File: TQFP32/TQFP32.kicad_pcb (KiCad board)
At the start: 2 copper layers, 20.1 x 40.6 mm, 8 parts, among them J1 Conn_01x16, J2 Conn_01x16, J3 Conn_02x16_Counter_Clockwise, J4 Conn_02x16_Counter_Clockwise

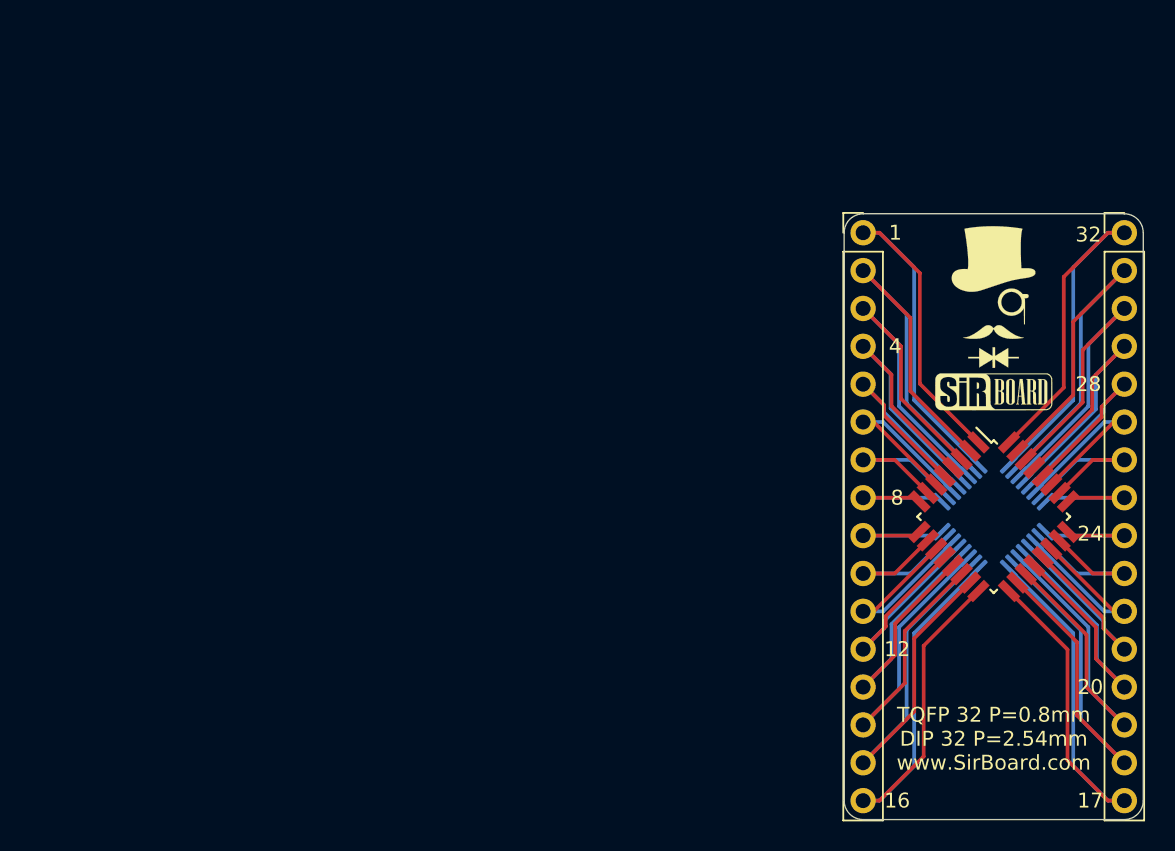
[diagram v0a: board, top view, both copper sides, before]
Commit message: Silkscreens and sizes updated
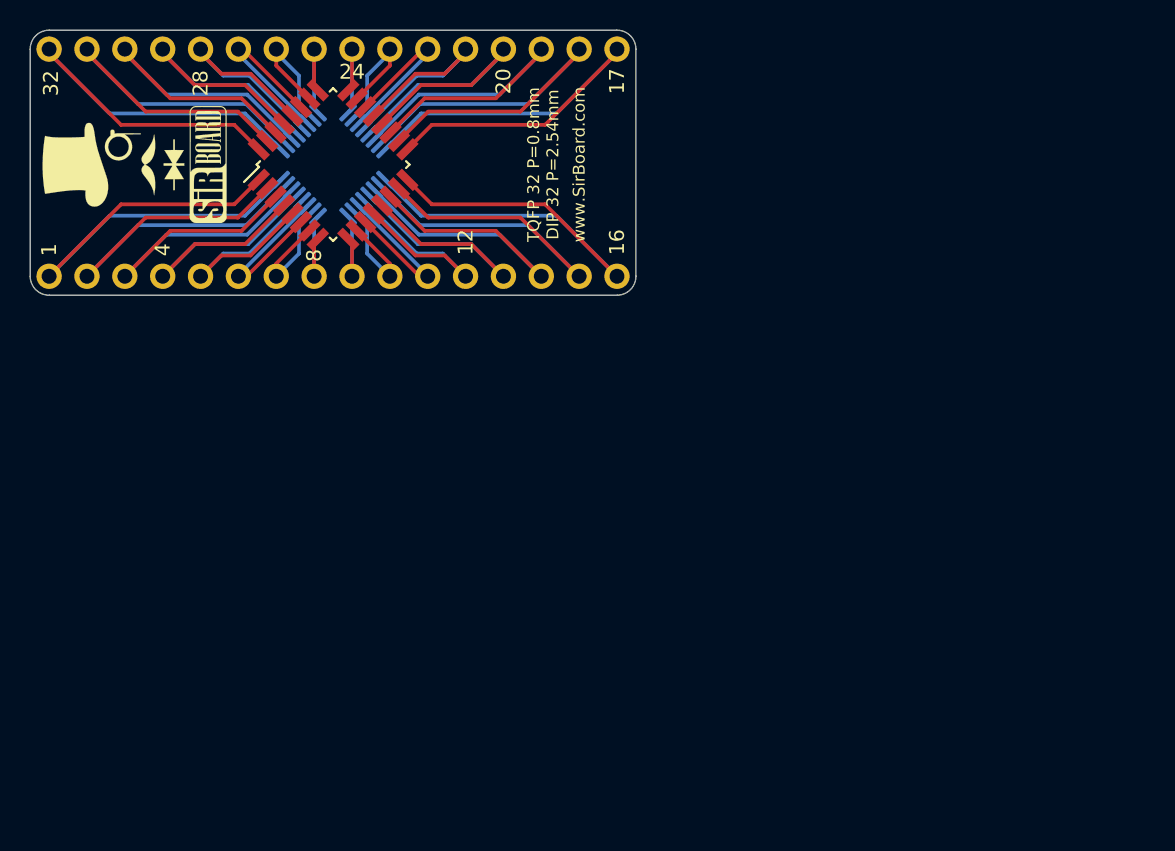
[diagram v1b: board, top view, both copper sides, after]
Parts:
- moved J2 73.2 mm to (136.1, 81.2), turned to 90 degrees
- moved G*** 59.7 mm to (140.5, 88.9), turned to 90 degrees
- moved G*** 54.9 mm to (146.8, 88.9), turned to 90 degrees
- moved J1 54.7 mm to (136.1, 96.4), turned to 90 degrees
- moved J3 50.2 mm to (155.2, 88.9), turned to 45 degrees
- moved J4 50.2 mm to (155.2, 88.9), turned to 135 degrees
- moved G*** 49.2 mm to (161.5, 88.9), turned to 90 degrees
- moved G*** 48.9 mm to (169.3, 88.9), turned to 90 degrees
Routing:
- net Net-(J1-Pad8): track 9.27 -> 6.73 mm
- net Net-(J1-Pad9): track 9.27 -> 6.73 mm
- net Net-(J2-Pad10): track 11.9 -> 9.37 mm
- net Net-(J1-Pad10): track 11.9 -> 9.37 mm
- net Net-(J2-Pad8): track 9.27 -> 6.73 mm
- net Net-(J2-Pad9): track 9.27 -> 6.73 mm
- net Net-(J2-Pad7): track 11.9 -> 9.37 mm
- net Net-(J1-Pad7): track 11.9 -> 9.37 mm
- net Net-(J1-Pad1): track 37.3 -> 35.0 mm
- net Net-(J1-Pad16): track 37.3 -> 35.0 mm
- net Net-(J2-Pad1): track 37.3 -> 35.0 mm
- net Net-(J2-Pad16): track 37.3 -> 35.0 mm
- net Net-(J2-Pad6): track 14.6 -> 12.3 mm
- net Net-(J2-Pad11): track 14.6 -> 12.3 mm
- net Net-(J1-Pad6): track 14.6 -> 12.3 mm
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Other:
- board size 20.1 x 40.6 mm -> 40.6 x 17.8 mm

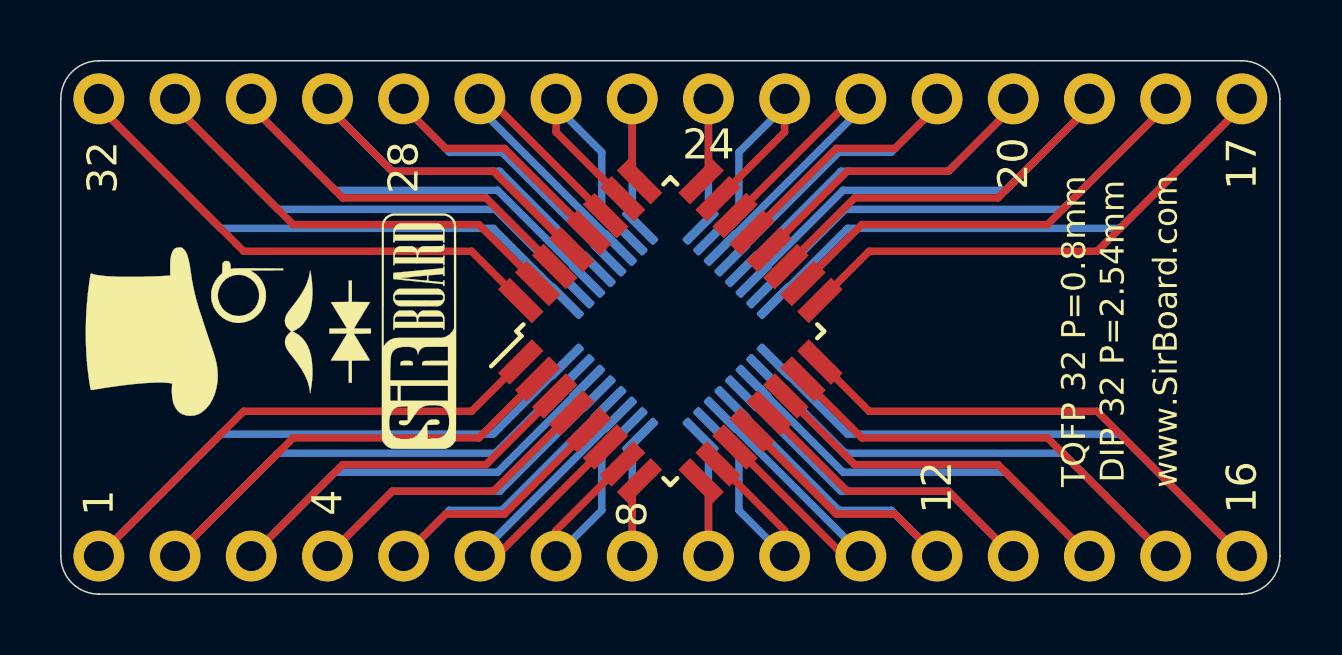
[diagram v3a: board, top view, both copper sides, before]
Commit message: Pin Numbering edited
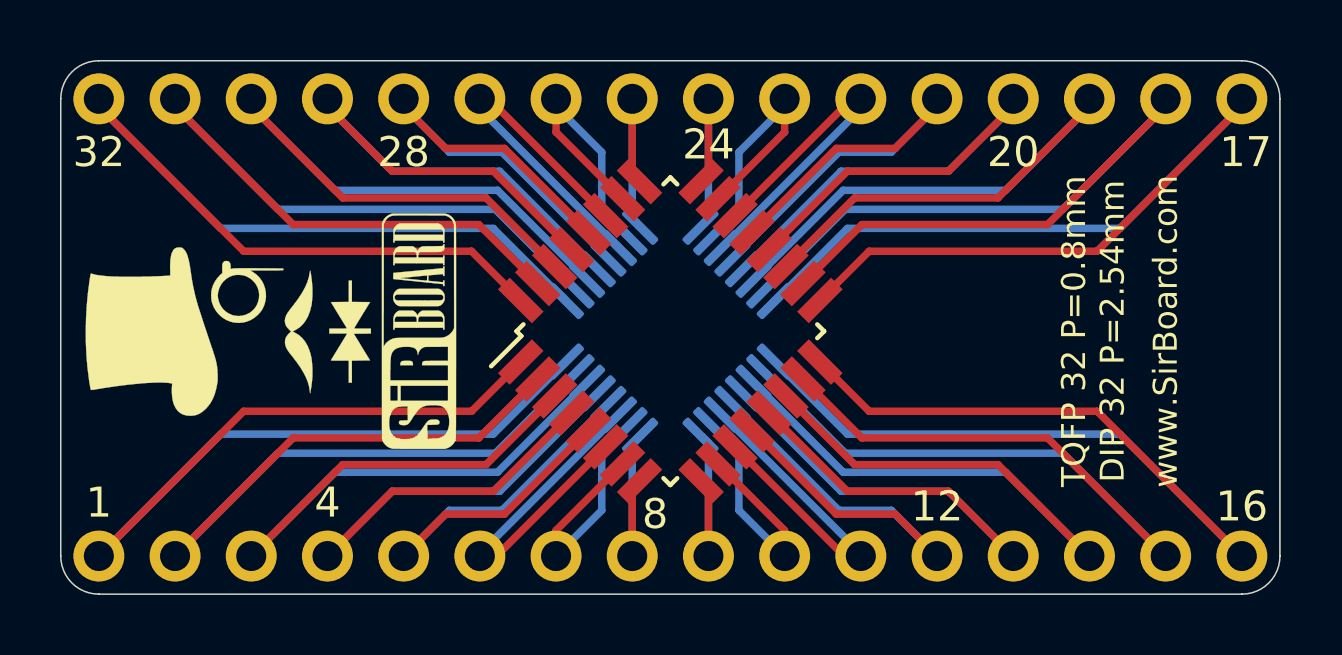
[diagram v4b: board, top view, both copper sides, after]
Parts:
- J1, J2: moved to B.Cu
- turned J1 to 270 degrees
- turned J2 to 270 degrees

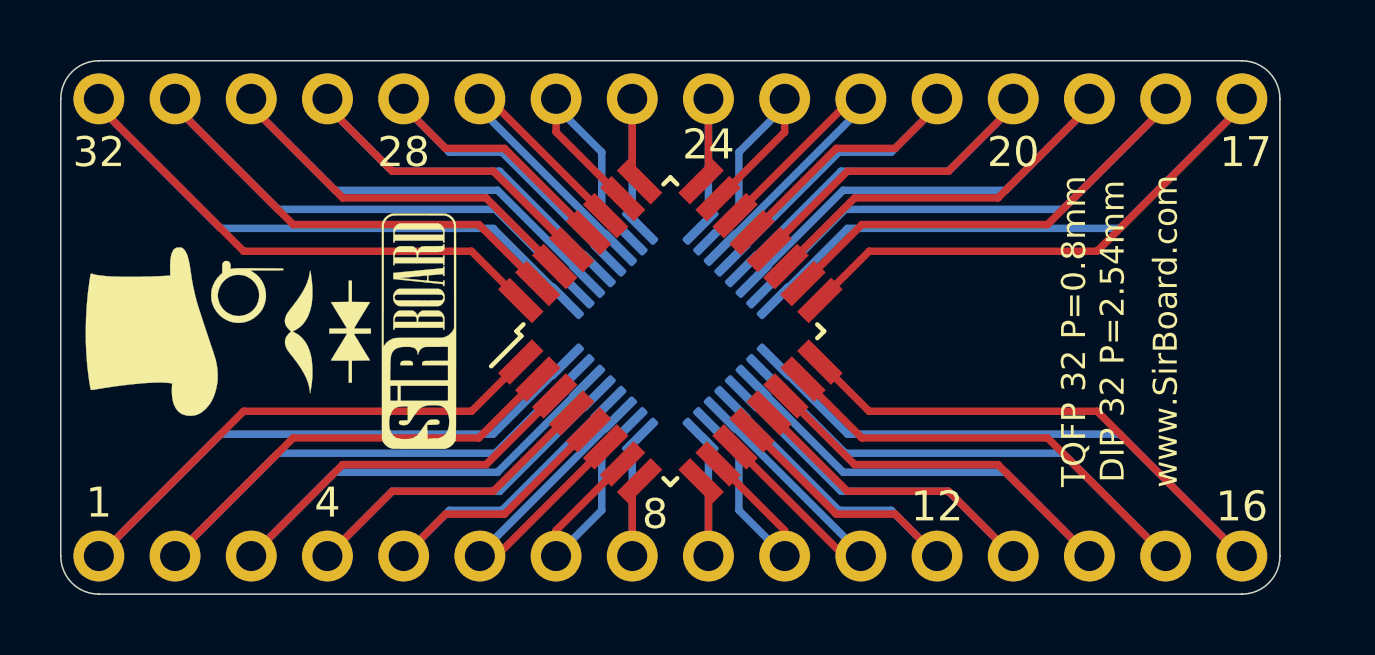
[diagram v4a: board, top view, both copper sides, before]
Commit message: Numbering Orientation Edited
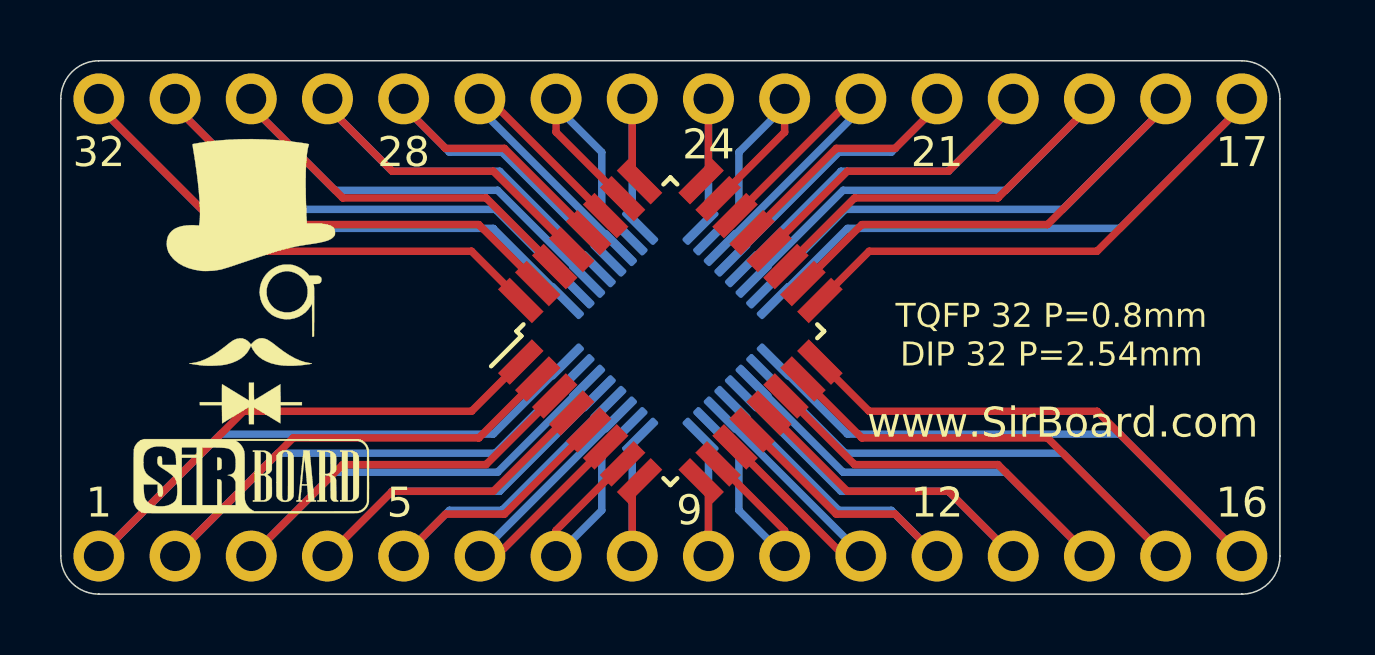
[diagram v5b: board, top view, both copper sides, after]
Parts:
- removed the G*** at (161.5, 88.9)
- added G***: LOGO, logo:SirBoard79x25, B.Cu at (169.2, 93.6)
- moved G*** 7.38 mm to (141.2, 93.7), turned to 0 degrees
- moved G*** 1.82 mm to (141.2, 87.2), turned to 0 degrees
- moved G*** 1.78 mm to (169.2, 87.1), turned to 180 degrees
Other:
- board text added: "21"
- board text added: "5"
- board text added: "9"
- board text removed: "20"
- board text removed: "4"
- board text removed: "8"

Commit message: Silkscreen Edits
Dimensions moved to Drawings Layer
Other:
- rule pad_to_mask_clearance: 0.051 -> 0
- rule solder_mask_min_width: 0.25 -> 0.1
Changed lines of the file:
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@@
     (pad_size 1.7 1.7)
     (pad_drill 1)
-    (pad_to_mask_clearance 0.051)
-    (solder_mask_min_width 0.25)
+    (pad_to_mask_clearance 0)
+    (solder_mask_min_width 0.1)
     (aux_axis_origin 0 0)
     (visible_elements 7FFFFFFF)
@@
       (usegerberadvancedattributes false)
       (creategerberjobfile false)
-      (excludeedgelayer false)
+      (excludeedgelayer true)
       (linewidth 0.100000)
       (plotframeref false)
       (viasonmask false)
       (mode 1)
-      (useauxorigin false)
+      (useauxorigin true)
       (hpglpennumber 1)
       (hpglpenspeed 20)
@@
       (psnegative false)
       (psa4output false)
-      (plotreference false)
-      (plotvalue true)
+      (plotreference true)
+      (plotvalue false)
       (plotinvisibletext false)
       (padsonsilk false)
@@
     )
   )
-  (dimension 38.1 (width 0.15) (layer F.SilkS)
-    (gr_text "38.100 mm" (at 155.194 77.567) (layer F.SilkS)
+  (dimension 38.1 (width 0.15) (layer Dwgs.User)
+    (gr_text "38.100 mm" (at 155.194 77.567) (layer Dwgs.User)
       (effects (font (size 1 1) (thickness 0.15)) hide)
     )
@@
     (arrow2b (pts (xy 136.144 78.867) (xy 137.270504 78.280579)))
   )
-  (dimension 40.64 (width 0.15) (layer F.SilkS)
-    (gr_text "40.640 mm" (at 155.194 74.773) (layer F.SilkS)
+  (dimension 40.64 (width 0.15) (layer Dwgs.User)
+    (gr_text "40.640 mm" (at 155.194 74.773) (layer Dwgs.User)
       (effects (font (size 1 1) (thickness 0.15)) hide)
     )
@@
     (arrow2b (pts (xy 134.874 76.073) (xy 136.000504 75.486579)))
   )
-  (dimension 15.24 (width 0.12) (layer F.SilkS)
-    (gr_text "15.240 mm" (at 131.318 88.773 90) (layer F.SilkS)
+  (dimension 15.24 (width 0.12) (layer Dwgs.User)
+    (gr_text "15.240 mm" (at 131.318 88.773 90) (layer Dwgs.User)
       (effects (font (size 1 1) (thickness 0.15)) hide)
     )
@@
     (arrow2b (pts (xy 132.588 96.393) (xy 132.001579 95.266496)))
   )
-  (dimension 17.78 (width 0.12) (layer F.SilkS)
-    (gr_text "17.780 mm" (at 128.778 88.773 90) (layer F.SilkS)
+  (dimension 17.78 (width 0.12) (layer Dwgs.User)
+    (gr_text "17.780 mm" (at 128.778 88.773 90) (layer Dwgs.User)
       (effects (font (size 1 1) (thickness 0.15)) hide)
     )

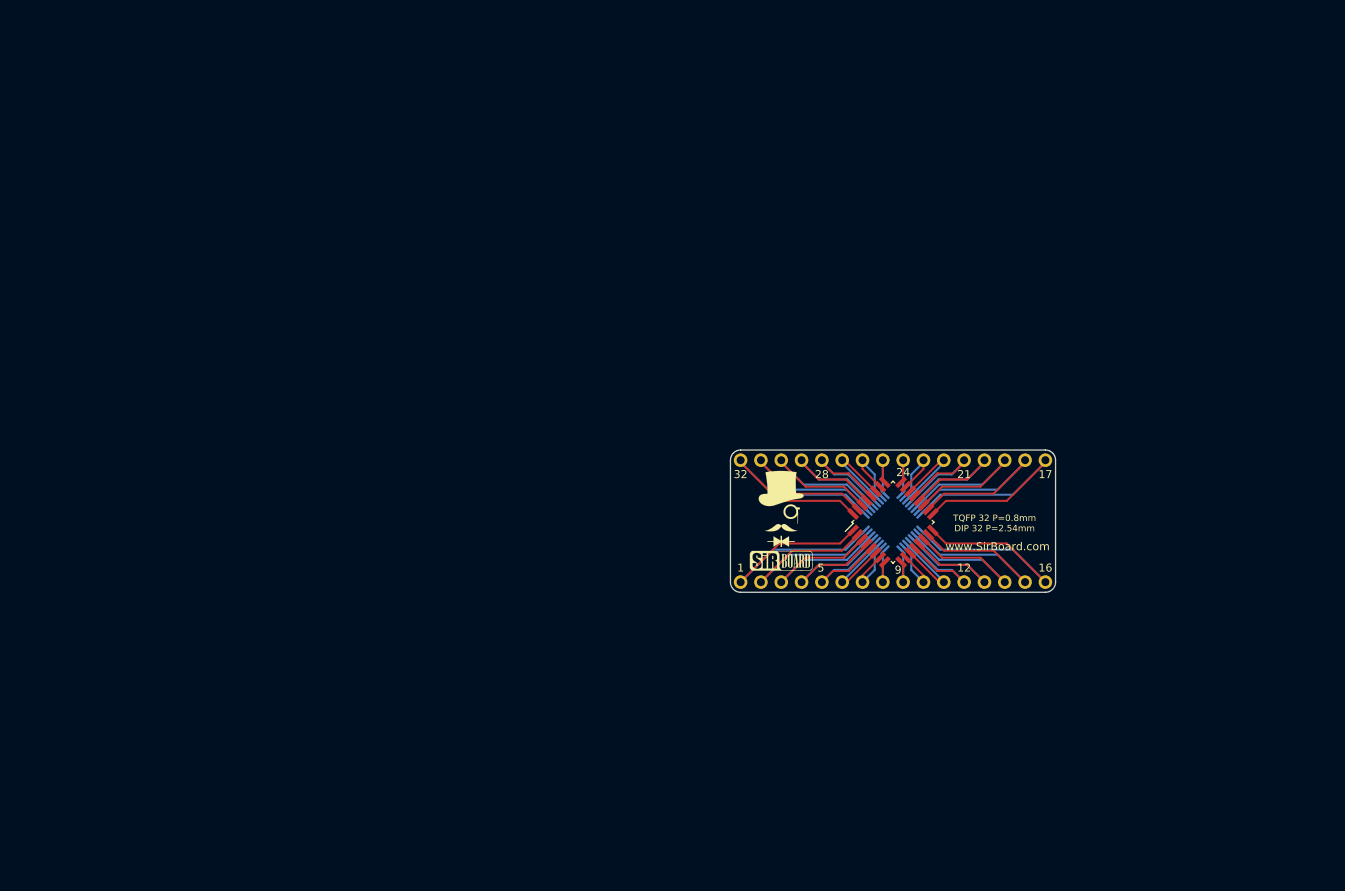
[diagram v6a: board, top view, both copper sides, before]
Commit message: USB, SD and CR Cells Added
MicroSD, MicroUSB, MiniUSB, USB-C, CR1220, CR2032 added as well as all schematics page sizes optimised
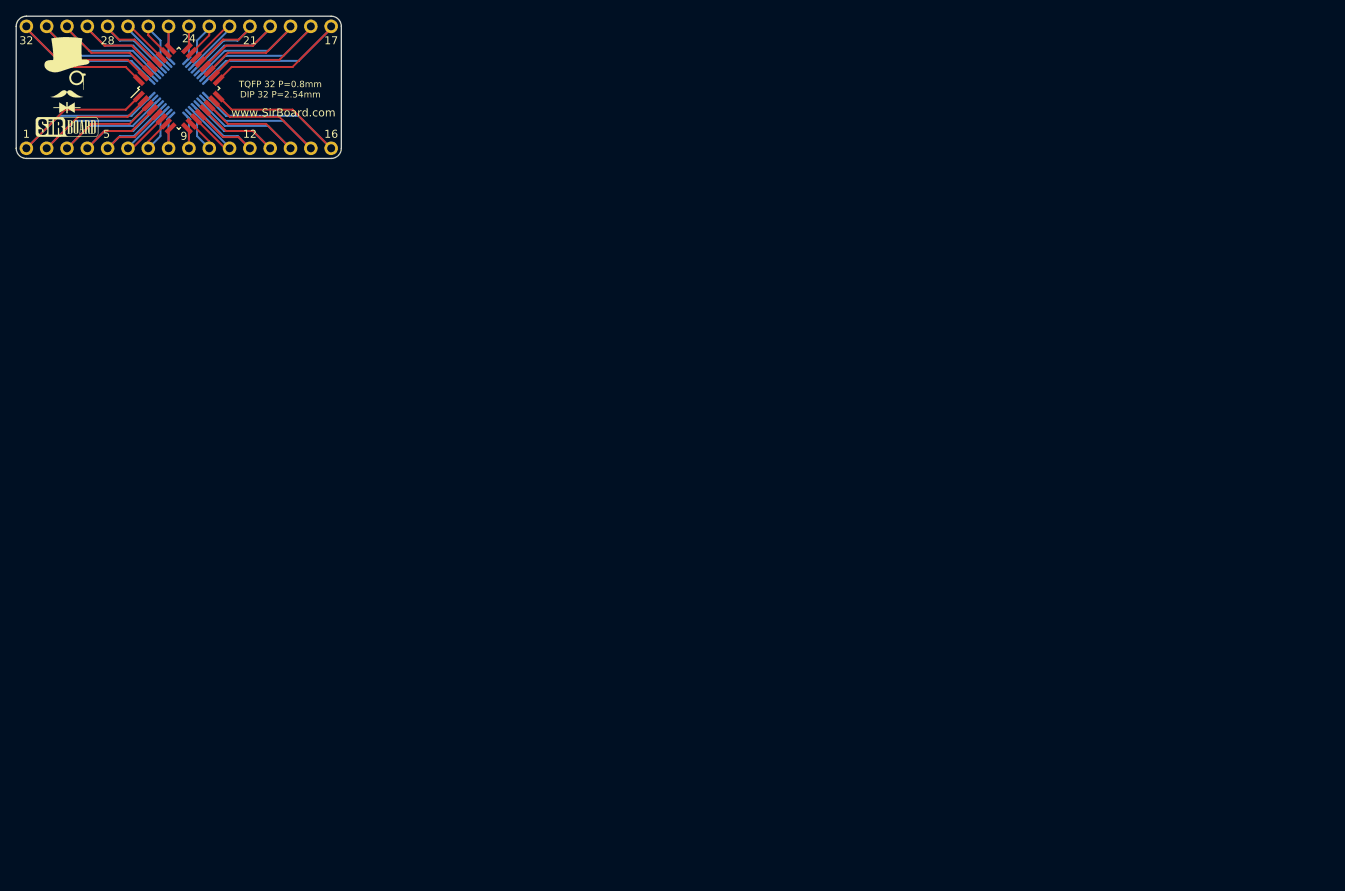
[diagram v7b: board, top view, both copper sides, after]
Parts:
- moved J1 104.5 mm to (46.9, 42.2)
- moved J2 104.5 mm to (46.9, 26.9)
- moved G*** 104.5 mm to (79.9, 39.4)
- moved G*** 104.5 mm to (79.9, 32.9)
- moved G*** 104.5 mm to (51.9, 39.5)
- moved G*** 104.5 mm to (51.9, 33.0)
- moved J3 104.5 mm to (65.9, 34.7)
- moved J4 104.5 mm to (65.9, 34.7)
